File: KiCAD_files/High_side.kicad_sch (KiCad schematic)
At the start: 28 parts, among them U602 ACS723LLCTR-20AB-T

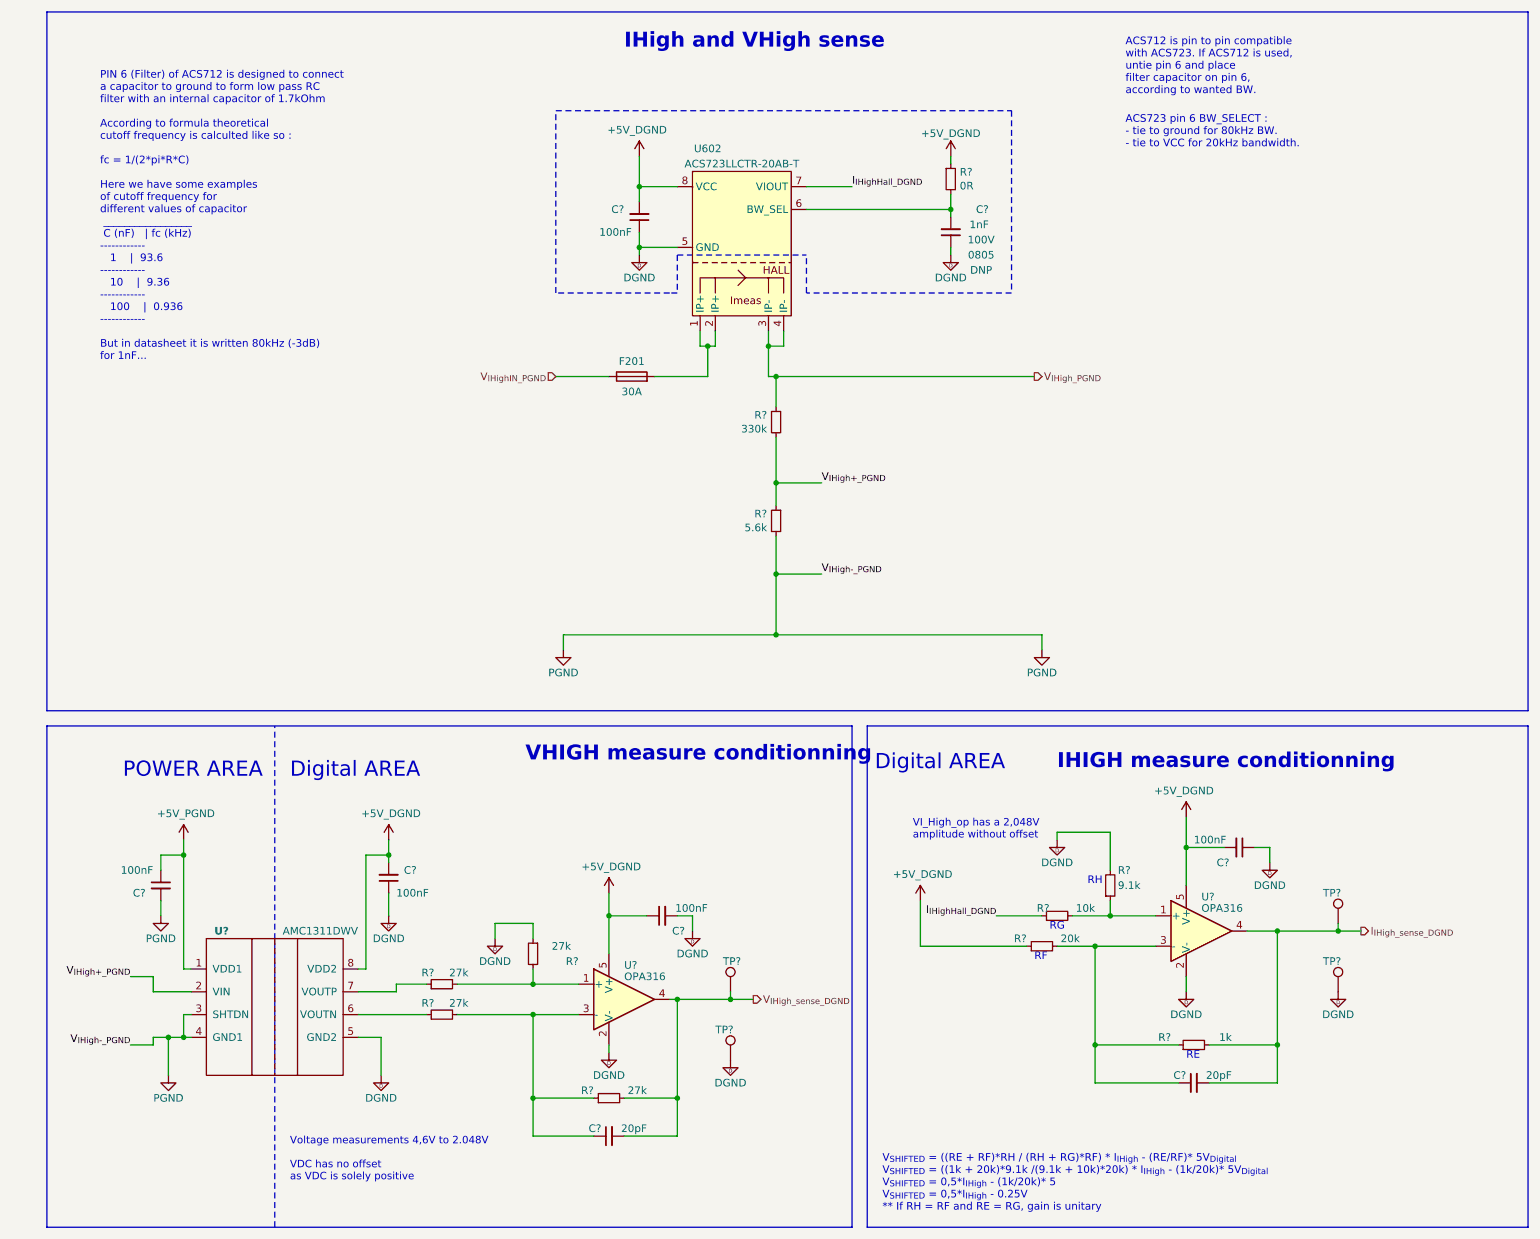
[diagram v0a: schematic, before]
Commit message: Added netclasses and ERC rules for isolation clearances
Signed-off-by: Jean Alinei <jean.alinei@laas.fr>
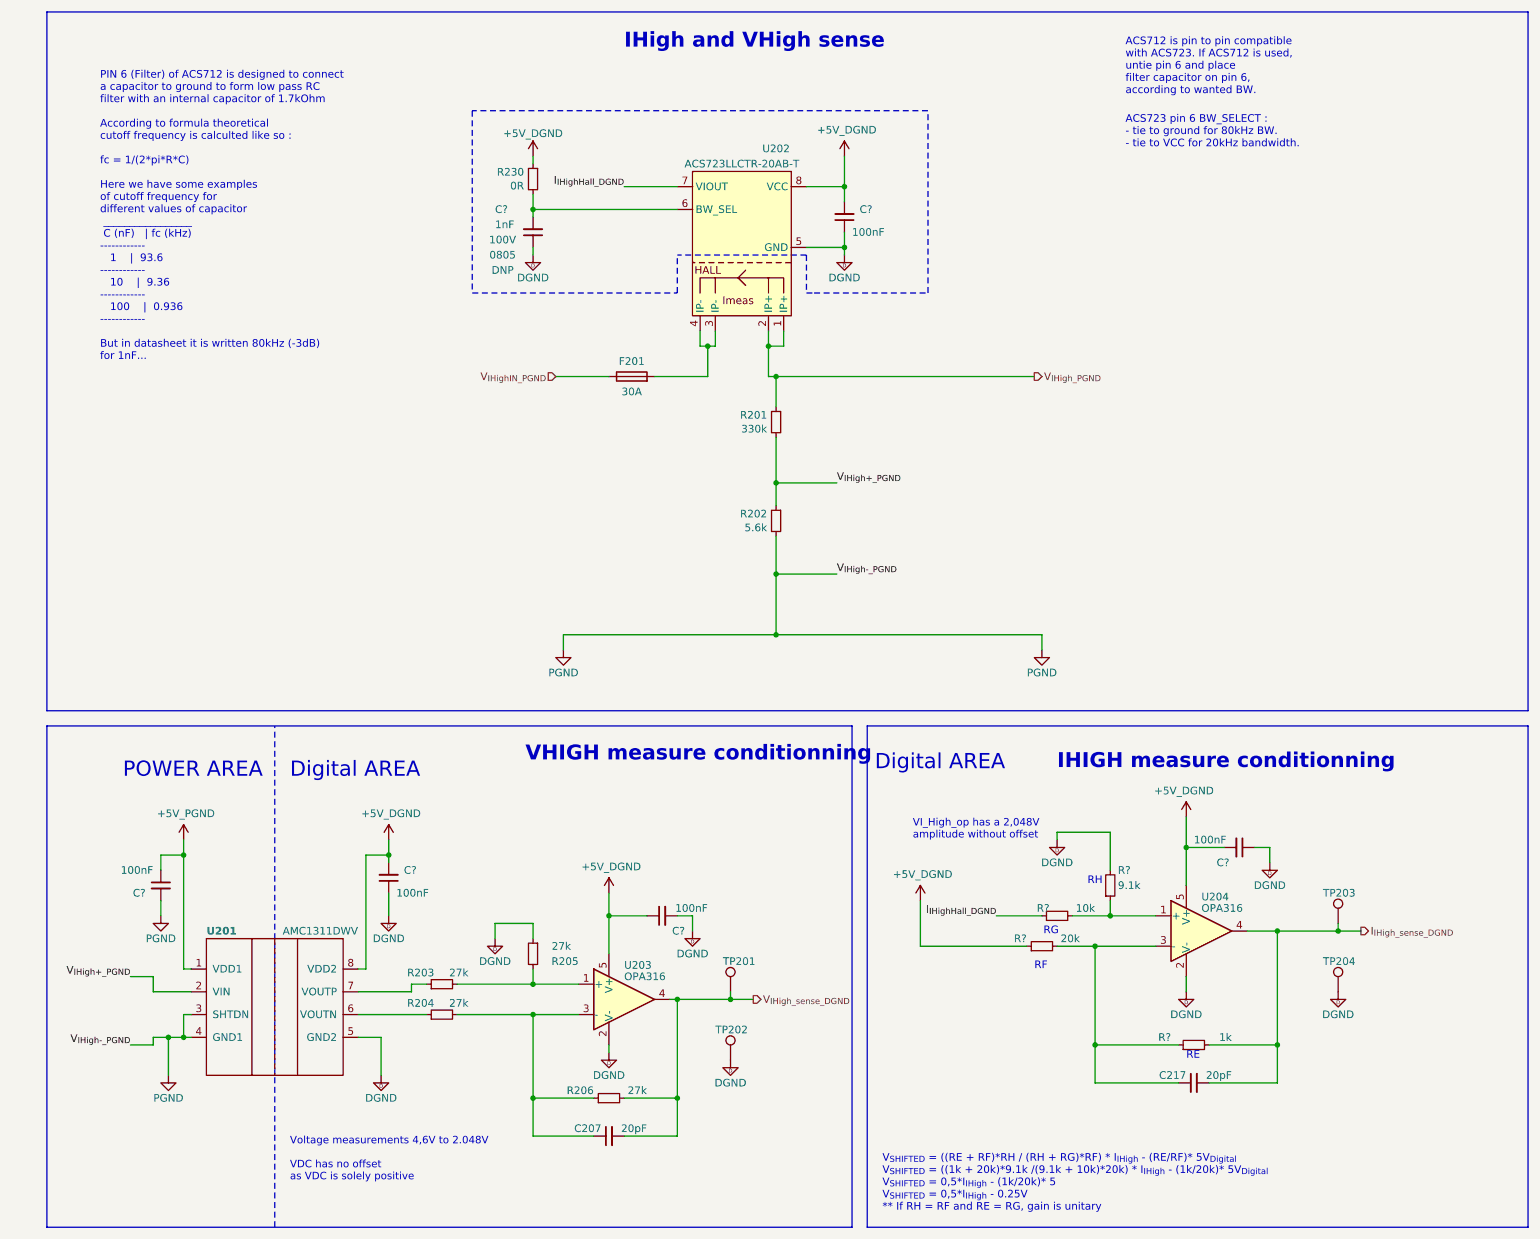
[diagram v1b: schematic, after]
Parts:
- gave numbers to parts that had none: 16
- renumbered U602 to U202
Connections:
- net V_{IHigh_PGND}: now also U202.1 (IP+), U202.2 (IP+); no longer U202.3 (IP-), U202.4 (IP-)
- new net: F201.2, U202.3 (IP-), U202.4 (IP-)
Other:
- moved on the sheet: C?, R230
